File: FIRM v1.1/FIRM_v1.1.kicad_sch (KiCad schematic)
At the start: 92 parts, among them J2 Conn_01x02_Pin, Q1 IRLML6402, U12 STM32F446ZCHx, U5 INA219AxDCN, U9 A-USBC-20F0-EA-GSR05, Y2 12 MHz

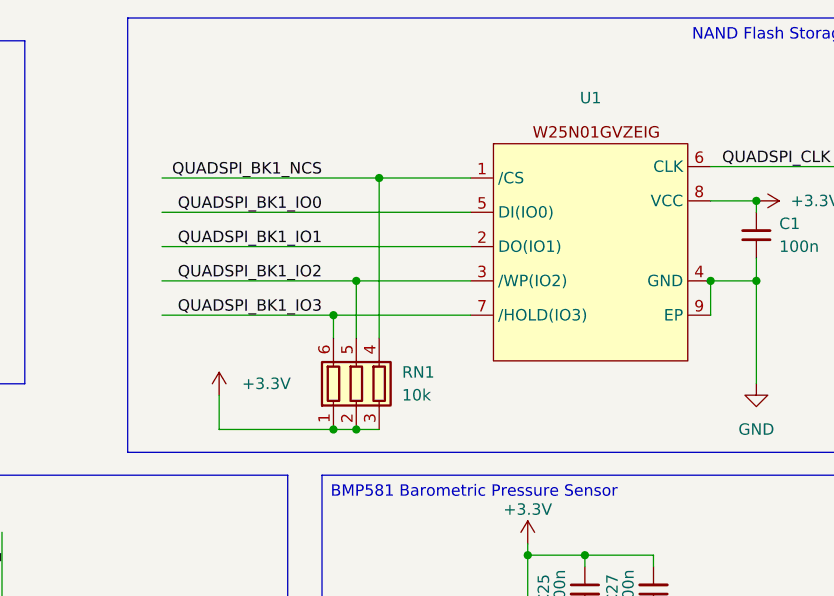
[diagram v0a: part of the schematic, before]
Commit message: Switched to W25N01KVZEIR
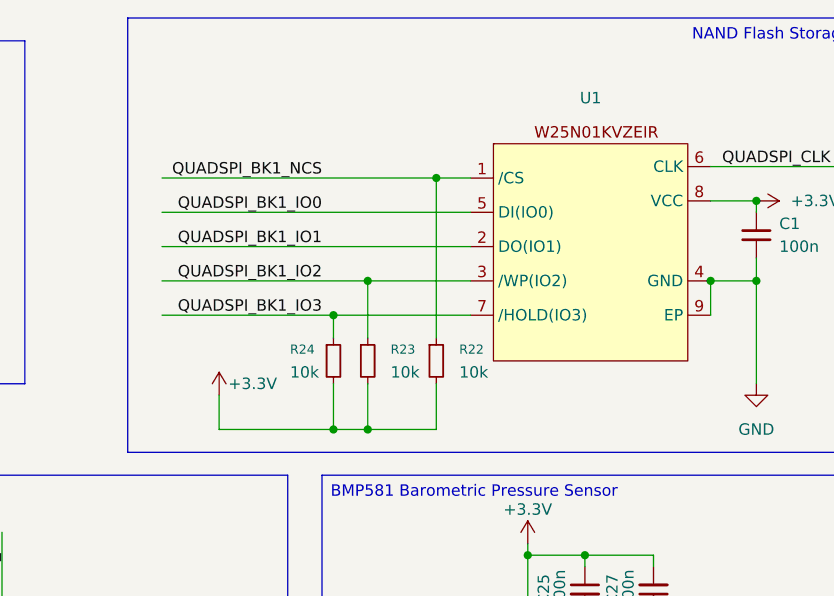
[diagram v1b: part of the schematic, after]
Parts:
- removed RN1: 10k, Resistor_THT:R_Array_SIP6, symbol Device:R_Pack03
- removed U1: (no value), Custom:W25N01GVZEIG, symbol Custom:W25N01GVZEIG
- added R22, R23, R24: 10k, Package_DIP:DIP-8_W7.62mm, symbol Device:R_Small
- added U1: (no value), HPRC_Storage:W25N01KVZEIR, symbol HPRC_Storage:W25N01KVZEIR
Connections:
- net +3.3V: now also R22.2, R23.2, R24.2, U1.8 (VCC)
- net GND: now also U1.4 (GND), U1.9 (EP)
- net QUADSPI_BK1_IO0: now also U1.5 (DI(IO0))
- net QUADSPI_BK1_IO1: now also U1.2 (DO(IO1))
- net QUADSPI_BK1_IO2: now also R23.1, U1.3 (/WP(IO2))
- net QUADSPI_BK1_IO3: now also R24.1, U1.7 (/HOLD(IO3))
- net QUADSPI_BK1_NCS: now also R22.1, U1.1 (/CS)
- net QUADSPI_CLK: now also U1.6 (CLK)

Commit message: Assigned all resistors and caps footprints
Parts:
- C1: footprint Package_SO:SOIC-8_3.9x4.9mm_P1.27mm -> Capacitor_SMD:C_0402_1005Metric
- C2, C3: footprint HPRC_Sensors:ADXL375BCCZ-RL7 -> Capacitor_SMD:C_0402_1005Metric
- R11, R12, R13, R14, R22, R23, R24, R3, R32, R4, R5: footprint Package_DIP:DIP-8_W7.62mm -> Resistor_SMD:R_0402_1005Metric
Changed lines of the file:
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@@
 			)
 		)
-		(property "Footprint" "Package_DIP:DIP-8_W7.62mm"
+		(property "Footprint" "Resistor_SMD:R_0402_1005Metric"
 			(at 167.64 152.4 0)
 			(hide yes)
@@
 			)
 		)
-		(property "Footprint" "Package_DIP:DIP-8_W7.62mm"
+		(property "Footprint" "Resistor_SMD:R_0402_1005Metric"
 			(at 405.13 52.07 0)
 			(hide yes)
@@
 			)
 		)
-		(property "Footprint" "Package_DIP:DIP-8_W7.62mm"
+		(property "Footprint" "Resistor_SMD:R_0402_1005Metric"
 			(at 255.27 172.72 0)
 			(hide yes)
@@
 			)
 		)
-		(property "Footprint" "HPRC_Sensors:ADXL375BCCZ-RL7"
+		(property "Footprint" "Capacitor_SMD:C_0402_1005Metric"
 			(at 331.47 151.13 0)
 			(hide yes)
@@
 			)
 		)
-		(property "Footprint" "Package_DIP:DIP-8_W7.62mm"
+		(property "Footprint" "Resistor_SMD:R_0402_1005Metric"
 			(at 416.56 52.07 0)
 			(hide yes)
@@
 			)
 		)
-		(property "Footprint" "Package_DIP:DIP-8_W7.62mm"
+		(property "Footprint" "Resistor_SMD:R_0402_1005Metric"
 			(at 408.94 52.07 0)
 			(hide yes)
@@
 			)
 		)
-		(property "Footprint" "Package_SO:SOIC-8_3.9x4.9mm_P1.27mm"
+		(property "Footprint" "Capacitor_SMD:C_0402_1005Metric"
 			(at 452.12 38.1 0)
 			(hide yes)
@@
 			)
 		)
-		(property "Footprint" "Package_DIP:DIP-8_W7.62mm"
+		(property "Footprint" "Resistor_SMD:R_0402_1005Metric"
 			(at 256.54 111.76 0)
 			(hide yes)
@@
 			)
 		)
-		(property "Footprint" "Package_DIP:DIP-8_W7.62mm"
+		(property "Footprint" "Resistor_SMD:R_0402_1005Metric"
 			(at 266.7 133.35 0)
 			(hide yes)
@@
 			)
 		)
-		(property "Footprint" "Package_DIP:DIP-8_W7.62mm"
+		(property "Footprint" "Resistor_SMD:R_0402_1005Metric"
 			(at 257.81 133.35 0)
 			(hide yes)
@@
 			)
 		)
-		(property "Footprint" "Package_DIP:DIP-8_W7.62mm"
+		(property "Footprint" "Resistor_SMD:R_0402_1005Metric"
 			(at 167.64 154.94 0)
 			(hide yes)
@@
 			)
 		)
-		(property "Footprint" "HPRC_Sensors:ADXL375BCCZ-RL7"
+		(property "Footprint" "Capacitor_SMD:C_0402_1005Metric"
 			(at 361.95 151.13 0)
 			(hide yes)
@@
 			)
 		)
-		(property "Footprint" "Package_DIP:DIP-8_W7.62mm"
+		(property "Footprint" "Resistor_SMD:R_0402_1005Metric"
 			(at 266.7 154.94 0)
 			(hide yes)
@@
 			)
 		)
-		(property "Footprint" "Package_DIP:DIP-8_W7.62mm"
+		(property "Footprint" "Resistor_SMD:R_0402_1005Metric"
 			(at 168.91 160.02 0)
 			(hide yes)

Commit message: Marked impedance caps for SPI as Do not Populate
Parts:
- C44, C49, C51, C56, C57, C58, C59, C60: now not fitted
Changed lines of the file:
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@@
 		(on_board yes)
 		(in_pos_files yes)
-		(dnp no)
+		(dnp yes)
 		(property "Reference" "C59"
 			(at 272.288 158.75 90)
@@
 		(on_board yes)
 		(in_pos_files yes)
-		(dnp no)
+		(dnp yes)
 		(property "Reference" "C51"
 			(at 155.448 163.83 90)
@@
 		(on_board yes)
 		(in_pos_files yes)
-		(dnp no)
+		(dnp yes)
 		(property "Reference" "C60"
 			(at 273.558 175.26 90)
@@
 		(on_board yes)
 		(in_pos_files yes)
-		(dnp no)
+		(dnp yes)
 		(property "Reference" "C44"
 			(at 140.208 163.83 90)
@@
 		(on_board yes)
 		(in_pos_files yes)
-		(dnp no)
+		(dnp yes)
 		(property "Reference" "C58"
 			(at 263.398 220.98 90)
@@
 		(on_board yes)
 		(in_pos_files yes)
-		(dnp no)
+		(dnp yes)
 		(property "Reference" "C56"
 			(at 257.048 158.75 90)
@@
 		(on_board yes)
 		(in_pos_files yes)
-		(dnp no)
+		(dnp yes)
 		(property "Reference" "C57"
 			(at 258.318 184.15 90)
@@
 		(on_board yes)
 		(in_pos_files yes)
-		(dnp no)
+		(dnp yes)
 		(property "Reference" "C49"
 			(at 147.828 163.83 90)

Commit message: SCH16T-K01-1 IMU added, needs review
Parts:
- added C61, C65: 100n, Capacitor_SMD:C_0402_1005Metric, symbol Device:C_Small
- added C62: 10u, Capacitor_SMD:C_0402_1005Metric, symbol Device:C_Small
- added C63, C64: 1u, Capacitor_SMD:C_0402_1005Metric, symbol Device:C_Small
- added R25: 10k, Resistor_SMD:R_0402_1005Metric, symbol Device:R
- added U11: SCH16T-K01-10, HPRC_Sensors:XDCR_SCH16T-K01-10, symbol HPRC_Sensors:SCH16T-K01-10
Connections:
- net +3.3V: now also C61.1, C64.1, C65.1, R25.1, U11.17 (V3P3), U11.18 (VDDIO), U11.8 (V3P3)
- net GND: now also C61.2, C62.2, C63.2, C64.2, C65.2, U11.1 (HEATSINK), U11.12 (GND), U11.13 (GND), U11.16 (GND), U11.24 (HEATSINK), U11.3 (TA9), U11.4 (TA8), U11.5 (RESERVED), U11.7 (RESERVED), U11.9 (GND)
- net MISO3: now also U11.19 (MISO)
- net MOSI3: now also U11.23 (MOSI)
- net SCK3: now also U11.21 (SCK)
- new net: C62.1, U11.10 (VREGA2), U11.11 (VREGA)
- new net: C63.1, U11.14 (VREGD2), U11.15 (VREGD)
- new net: R25.2, U11.6 (~{EXTRES})
- new net IMUL_CS: U11.22 (CS)
- new net IMUL_INT: U11.20 (DRY_SYNC)
- no-connect marks 17 -> 18

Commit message: Added IMUL_CS and IMUL_INT
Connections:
- net IMUL_CS: now also U12.K11 (PD14)
- net IMUL_INT: now also U12.K10 (PD13)
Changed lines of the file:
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@@
+	(wire
+		(pts
+			(xy 251.46 228.6) (xy 260.35 228.6)
+		)
+		(stroke
+			(width 0)
+			(type default)
+		)
+	)
 	(wire
 		(pts
@@
 		(pts
 			(xy 353.06 146.05) (xy 353.06 156.21)
+		)
+		(stroke
+			(width 0)
+			(type default)
+		)
+	)
+	(wire
+		(pts
+			(xy 251.46 226.06) (xy 260.35 226.06)
 		)
 		(stroke
@@
 		)
 	)
+	(label "IMUL_CS"
+		(at 260.35 228.6 180)
+		(effects
+			(font
+				(size 1.27 1.27)
+			)
+			(justify right bottom)
+		)
+	)
 	(label "MOSI2"
 		(at 440.69 116.84 90)
@@
 		)
 	)
+	(label "IMUL_INT"
+		(at 260.35 226.06 180)
+		(effects
+			(font
+				(size 1.27 1.27)
+			)
+			(justify right bottom)
+		)
+	)

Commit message: Fixed Errors and switched out Regulator
I tackled errors described in the pull request. I also switched out the regulator . I need to still fix all ERC warnings and pick out a part for our inductor in the regulator.
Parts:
- removed C24, C28: 10u, Capacitor_SMD:C_0402_1005Metric, symbol Device:C_Small
- removed C44, C49, C51, C56, C57, C58, C59, C60: pad, Capacitor_SMD:C_0402_1005Metric, symbol Device:C_Small
- removed Q1: IRLML6402, Package_TO_SOT_SMD:SOT-23, symbol Transistor_FET:IRLML6402
- removed R19: 100k, Resistor_SMD:R_0402_1005Metric, symbol Device:R_Small
- removed TP1: 3.3V Test Point, connectors:Testpoint_1.5x1.5mm_1.0mm, symbol Connector:TestPoint
- removed TP2: GND Test Point, connectors:Testpoint_1.5x1.5mm_1.0mm, symbol Connector:TestPoint
- removed TP3: UART_RX Test Point, connectors:Testpoint_1.5x1.5mm_1.0mm, symbol Connector:TestPoint
- removed TP4: UART_TX Test Point, connectors:Testpoint_1.5x1.5mm_1.0mm, symbol Connector:TestPoint
- removed TP6: SWDIO Through-Hole, connectors:Testpoint_1.5x1.5mm_1.0mm, symbol Connector:TestPoint
- removed TP7: SWCLK Through-Hole, connectors:Testpoint_1.5x1.5mm_1.0mm, symbol Connector:TestPoint
- removed U3: (no value), HPRC_regulators:MIC5216-3.3M5, symbol HPRC_Regulators:MIC5216-3.3YM5-TR
- added C26: 10u, Capacitor_SMD:C_0201_0603Metric, symbol Device:C_Small
- added C31: 22u, Capacitor_SMD:C_0201_0603Metric, symbol Device:C_Small
- added C56, C57, C59: 1u, Capacitor_SMD:C_0402_1005Metric, symbol Device:C
- added C58: 100n, Capacitor_SMD:C_0402_1005Metric, symbol Device:C
- added J1: Pin, Connector_PinHeader_1.00mm:PinHeader_1x06_P1.00mm_Vertical, symbol Connector:Conn_01x06_Pin
- added L1: 2u2, symbol Device:L_Small
- added PS1: TPS62162DSGR, TPS62162DSGR:SON50P200X200X80-9N, symbol HPRC_Regulators:TPS62162DSGR
- added Q2: DMP3098L-7, HPRC_Logic:DMP3098L-7, symbol HPRC_Logic_ICs:DMP3098L-7
- added R26: 100k, Resistor_SMD:R_0402_1005Metric, symbol Device:R_Small
- C2: footprint Capacitor_SMD:C_0402_1005Metric -> Capacitor_Tantalum_SMD:CP_EIA-1608-08_AVX-J
- C46, C47: Digikey PN 490-GJM1555C1H140FB01DCT-ND -> GJM1555C1H100GB01D
- R1, R15, R33, R34, R9: footprint Package_DIP:DIP-8_W7.62mm -> Resistor_SMD:R_0201_0603Metric
- R11, R12, R13, R14, R3, R32: footprint Resistor_SMD:R_0402_1005Metric -> Resistor_SMD:R_0201_0603Metric
- R17: value 10m -> 100m
- Y1: renamed from Y2; footprint Crystal:Crystal_SMD_3225-4Pin_3.2x2.5mm -> connectors:Crystal_ECS-120-10-36B2-CWY-TR; Digikey PN 644-STDCRG2-25MCT-ND -> 50-ECS-120-10-36B2-CWY-TRCT-ND
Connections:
- net DEBUG0 is gone; now on net DEBUG_0: U12.A4 (PE1)
- net DEBUG1 is gone; now on net DEBUG_1: U12.A3 (PE2)
- net DEBUG2 is gone; now on net DEBUG_2: U12.A2 (PE3)
- net I2C1_SDL is gone; now on net I2C1_SCL: U2.14 (SCL/SCLK)
- net +3.3V: now also U12.L1 (VREF+), C31.1, C56.1, C57.1, C58.1, C59.1, J1.6 (Pin_6), L1.2, PS1.6 (VOS), R26.1
- net GND: now also U12.K1 (VREF-), C26.2, C31.2, C56.2, C57.2, C58.2, C59.2, J1.5 (Pin_5), PS1.1 (PGND), PS1.4 (AGND), PS1.5 (FB), PS1.9 (EXP)
- net SYS_JTCK-SWCLK: now also J1.3 (Pin_3)
- net SYS_JTMS-SWDIO: now also J1.4 (Pin_4)
- net USART1_RX: now also J1.2 (Pin_2)
- net USART1_TX: now also J1.1 (Pin_1)
- net VBAT: now also Q2.3
- net VBUS: now also Q2.1
- net VSENS_IN: now also Q2.2
- net VSENS_OUT: now also C26.1, PS1.2 (VIN), PS1.3 (EN)
- new net: PS1.8 (PG), R26.2
- new net: L1.1, PS1.7 (SW)
- no-connect marks 18 -> 94
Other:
- moved on the sheet: C12, C34, C39, C4, C40, C41, C42, C43, C45, C46, C47, C48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

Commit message: Got rid of ERC errors, switched out capacitors packaging for regulator, and chose out a murata inductor for regulator
Inductor chosen:
https://www.murata.com/~/media/webrenewal/products/inductor/chip/tokoproducts/wirewoundmetalalloychiptype/m_dfe252012f.ashx
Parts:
- added J3: FIRM2 Conn, Connector_PinHeader_1.00mm:PinHeader_1x02_P1.00mm_Vertical, symbol Connector:Conn_01x02_Pin
- C26, C31: footprint Capacitor_SMD:C_0201_0603Metric -> Capacitor_SMD:C_0603_1608Metric
- D12: value LED_Red -> LED_Green; Digikey PN 160-LTST-C281KRKTCT-ND -> 160-LTST-C281KGKTCT-ND
- D4: footprint connectors:D_schottky_NSR05F30NXT5G -> HPRC_Connectors:D_schottky_NSR05F30NXT5G
- J2: footprint connectors:power_headers -> HPRC_Connectors:power_headers
- L1: footprint (none) -> Inductor_SMD:L_1008_2520Metric
- PS1: footprint TPS62162DSGR:SON50P200X200X80-9N -> HPRC_Regulators:TPS62162DSGR
- U4: footprint sensors:IC_ICM-45686 -> HPRC_Sensors:IC_ICM-45686; symbol sensors:ICM-45686 -> HPRC_Sensors:ICM-45686
- U7: footprint sensors:BMPFootprintNoSolderMask -> HPRC_Sensors:BMP581; symbol sensors:BMP581 -> HPRC_Sensors:BMP581
- U8: footprint sensors:IC_MMC5983MA -> HPRC_Sensors:IC_MMC5983MA; symbol sensors:MMC5983MA -> HPRC_Sensors:MMC5983MA
- U9: footprint connectors:A-USBC-20F0-EA-GSR05 -> HPRC_Connectors:A-USBC-20F0-EA-GSR05; symbol connectors:A-USBC-20F0-EA-GSR05 -> HPRC_Connectors:A-USBC-20F0-EA-GSR05
- Y1: footprint connectors:Crystal_ECS-120-10-36B2-CWY-TR -> HPRC_Connectors:Crystal_ECS-120-10-36B2-CWY-TR
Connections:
- net USART2_RX: now also J3.1 (Pin_1)
- net USART2_TX: now also J3.2 (Pin_2)
- net HIG_CS: no longer names the net of U12.G11 (PG8)
- no-connect marks 94 -> 95

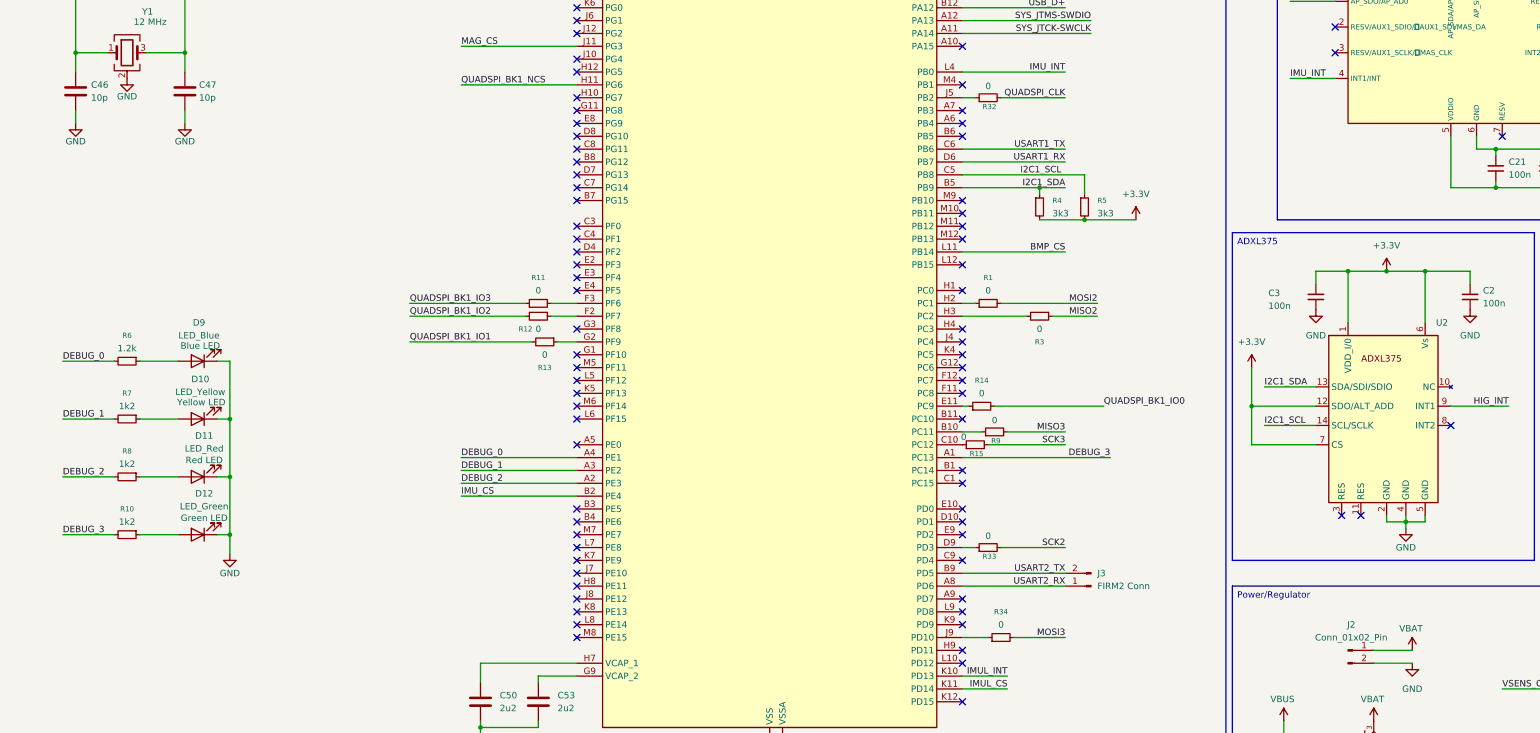
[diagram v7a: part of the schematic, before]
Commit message: Fixed ADXL375 , and SPI3 line pin out
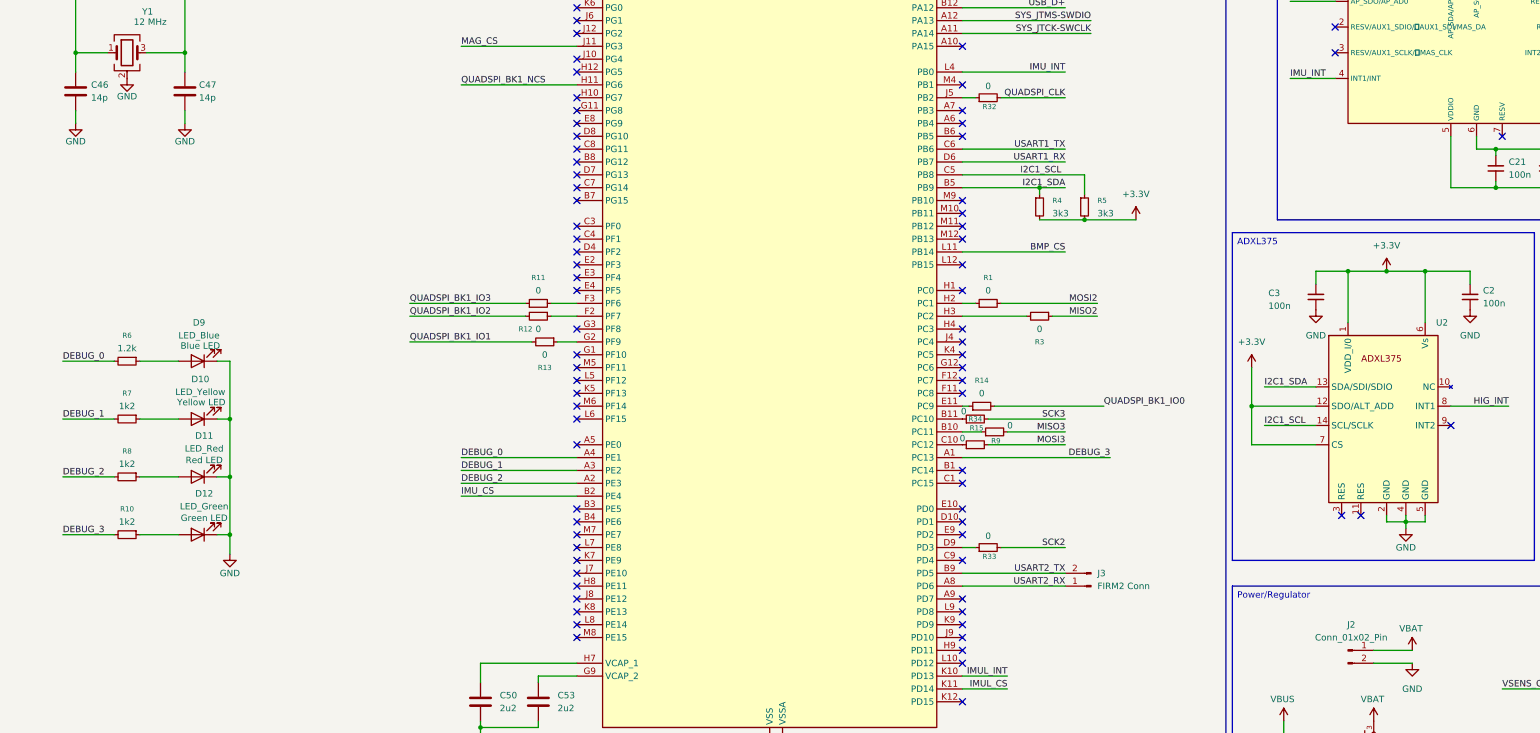
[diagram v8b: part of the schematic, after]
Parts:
- C46, C47: value 10p -> 14p
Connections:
- net HIG_INT: now also U2.8 (INT1); no longer U2.9 (INT1)
- net at R15.1: now also U12.B11 (PC10); no longer U12.C10 (PC12)
- net at R34.1: now also U12.C10 (PC12); no longer U12.J9 (PD10)
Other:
- moved on the sheet: R15, R34
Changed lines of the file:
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@@
 	)
 	(no_connect
-		(at 261.62 175.26)
+		(at 261.62 218.44)
 	)
 	(no_connect
@@
 	(wire
 		(pts
-			(xy 266.7 180.34) (xy 281.94 180.34)
+			(xy 266.7 175.26) (xy 281.94 175.26)
 		)
 		(stroke
@@
 	(wire
 		(pts
-			(xy 271.78 218.44) (xy 281.94 218.44)
-		)
-		(stroke
-			(width 0)
-			(type default)
-		)
-	)
-	(wire
-		(pts
-			(xy 261.62 218.44) (xy 266.7 218.44)
+			(xy 266.7 180.34) (xy 281.94 180.34)
 		)
 		(stroke
@@
 	)
 	(label "MOSI3"
-		(at 281.94 218.44 180)
+		(at 281.94 180.34 180)
 		(effects
 			(font
@@
 	)
 	(label "SCK3"
-		(at 281.94 180.34 180)
+		(at 281.94 175.26 180)
 		(effects
 			(font
@@
 	(symbol
 		(lib_id "Device:R_Small")
-		(at 264.16 180.34 90)
+		(at 264.16 175.26 90)
 		(unit 1)
 		(body_style 1)
@@
 		(dnp no)
 		(property "Reference" "R15"
-			(at 264.414 182.118 90)
+			(at 264.414 177.038 90)
 			(show_name no)
 			(do_not_autoplace no)
@@
 		)
 		(property "Value" "0"
-			(at 261.874 178.816 90)
+			(at 261.874 173.736 90)
 			(show_name no)
 			(do_not_autoplace no)
@@
 		)
 		(property "Footprint" "Resistor_SMD:R_0201_0603Metric"
-			(at 264.16 180.34 0)
+			(at 264.16 175.26 0)
 			(hide yes)
 			(show_name no)
@@
 		)
 		(property "Datasheet" ""
-			(at 264.16 180.34 0)
+			(at 264.16 175.26 0)
 			(hide yes)
 			(show_name no)
@@
 		)
 		(property "Description" "Resistor, small symbol"
-			(at 264.16 180.34 0)
+			(at 264.16 175.26 0)
 			(hide yes)
 			(show_name no)
@@
 			)
 		)
-		(property "Value" "10p"
+		(property "Value" "14p"
 			(at 110.744 111.76 0)
 			(show_name no)
@@
 	(symbol
 		(lib_id "Device:R_Small")
-		(at 269.24 218.44 90)
+		(at 264.16 180.34 90)
 		(unit 1)
 		(body_style 1)
@@
 		(dnp no)
 		(property "Reference" "R34"
-			(at 269.24 213.36 90)
+			(at 264.16 175.26 90)
 			(show_name no)
 			(do_not_autoplace no)
@@
 		)
 		(property "Value" "0"
-			(at 269.24 215.9 90)
+			(at 261.62 179.07 90)
 			(show_name no)
 			(do_not_autoplace no)
@@
 		)
 		(property "Footprint" "Resistor_SMD:R_0201_0603Metric"
-			(at 269.24 218.44 0)
+			(at 264.16 180.34 0)
 			(hide yes)
 			(show_name no)
@@
 		)
 		(property "Datasheet" ""
-			(at 269.24 218.44 0)
+			(at 264.16 180.34 0)
 			(hide yes)
 			(show_name no)
@@
 		)
 		(property "Description" "Resistor, small symbol"
-			(at 269.24 218.44 0)
+			(at 264.16 180.34 0)
 			(hide yes)
 			(show_name no)
@@
 		)
 		(property "Value" "0"
-			(at 267.97 175.514 90)
+			(at 271.018 176.53 90)
 			(show_name no)
 			(do_not_autoplace no)
@@
 			)
 		)
-		(property "Value" "10p"
+		(property "Value" "14p"
 			(at 89.408 111.76 0)
 			(show_name no)
